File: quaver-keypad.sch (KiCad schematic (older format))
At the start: 14 parts

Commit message: MCU schematic fix
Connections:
- wire segments 51 -> 45
- no-connect marks 2 -> 0
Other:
- moved on the sheet: C?, R?, SW?, U?, Y?

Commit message: schematics finished
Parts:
- added D1, D2, D3, D4: D_Small, Diode_SMD:D_SOD-123, symbol Device:D_Small
- added F1: 500mA, Fuse:Fuse_1206_3216Metric, symbol Device:Polyfuse
- added MX1, MX2, MX3, MX4: MX-NoLED, MX_Alps_Hybrid:MX-1U, symbol MX_Alps_Hybrid:MX-NoLED
- added USB1: Molex-0548190589, random-keyboard-parts:Molex-0548190589, symbol random-keyboard-parts:Molex-0548190589
- C1, C2, C3, C4, C5, C6, C7: renamed from C?; footprint (none) -> Capacitor_SMD:C_0805_2012Metric
- R1, R2, R3, R4: renamed from R?; footprint (none) -> Resistor_SMD:R_0805_2012Metric
- SW1: renamed from SW?; footprint (none) -> random-keyboard-parts:SKQG-1155865
- Y1: renamed from Y?; footprint (none) -> Crystal:Crystal_SMD_3225-4Pin_3.2x2.5mm
- gave numbers to parts that had none: 1
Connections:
- net +5V: now also F1.1; no longer U1.24 (AVCC), U1.44 (AVCC)
- net D+: now also USB1.3 (D+)
- net D-: now also USB1.4 (D-)
- net GND: now also USB1.1 (GND); no longer U1.15 (GND), U1.23 (GND), U1.35 (GND), U1.43 (GND)
- net ROW0: now reaches U1.27 (PD7)
- net ROW0: now also D1.1 (K), D3.1 (K)
- net COL1: now reaches U1.28 (PB4)
- net COL1: now also MX3.1 (COL), MX4.1 (COL)
- net COL0: now reaches U1.29 (PB5)
- net COL0: now also MX1.1 (COL), MX2.1 (COL)
- net ROW1: now reaches U1.30 (PB6)
- net ROW1: now also D2.1 (K), D4.1 (K)
- new net: U1.15 (GND), U1.23 (GND), U1.35 (GND), U1.43 (GND)
- new net: U1.24 (AVCC), U1.44 (AVCC)
- new net: D1.2 (A), MX1.2 (ROW)
- new net: D3.2 (A), MX3.2 (ROW)
- new net: D2.2 (A), MX2.2 (ROW)
- new net: D4.2 (A), MX4.2 (ROW)
- new net VCC: F1.2, USB1.5 (VBUS)
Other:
- moved on the sheet: C1, C2, C3, C4, C5, C6, C7, R1, R2, R3, R4, SW1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

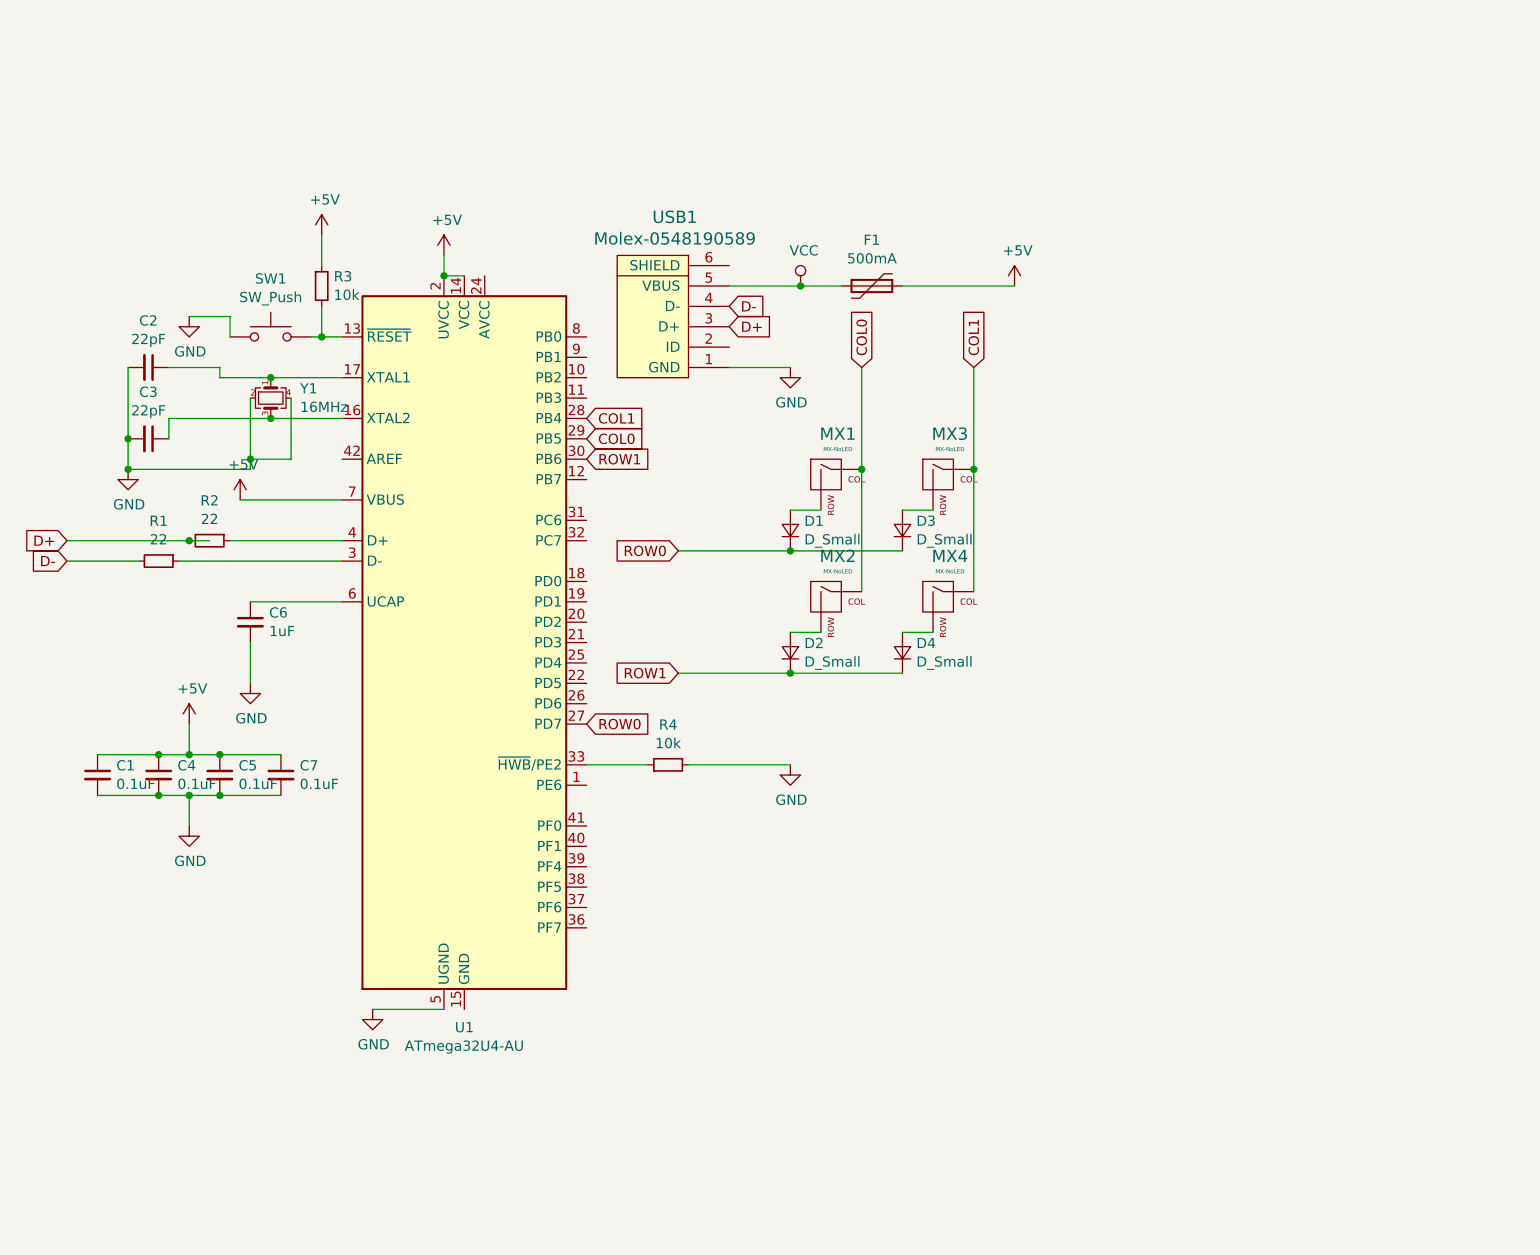
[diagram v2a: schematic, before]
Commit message: fixed mx keys
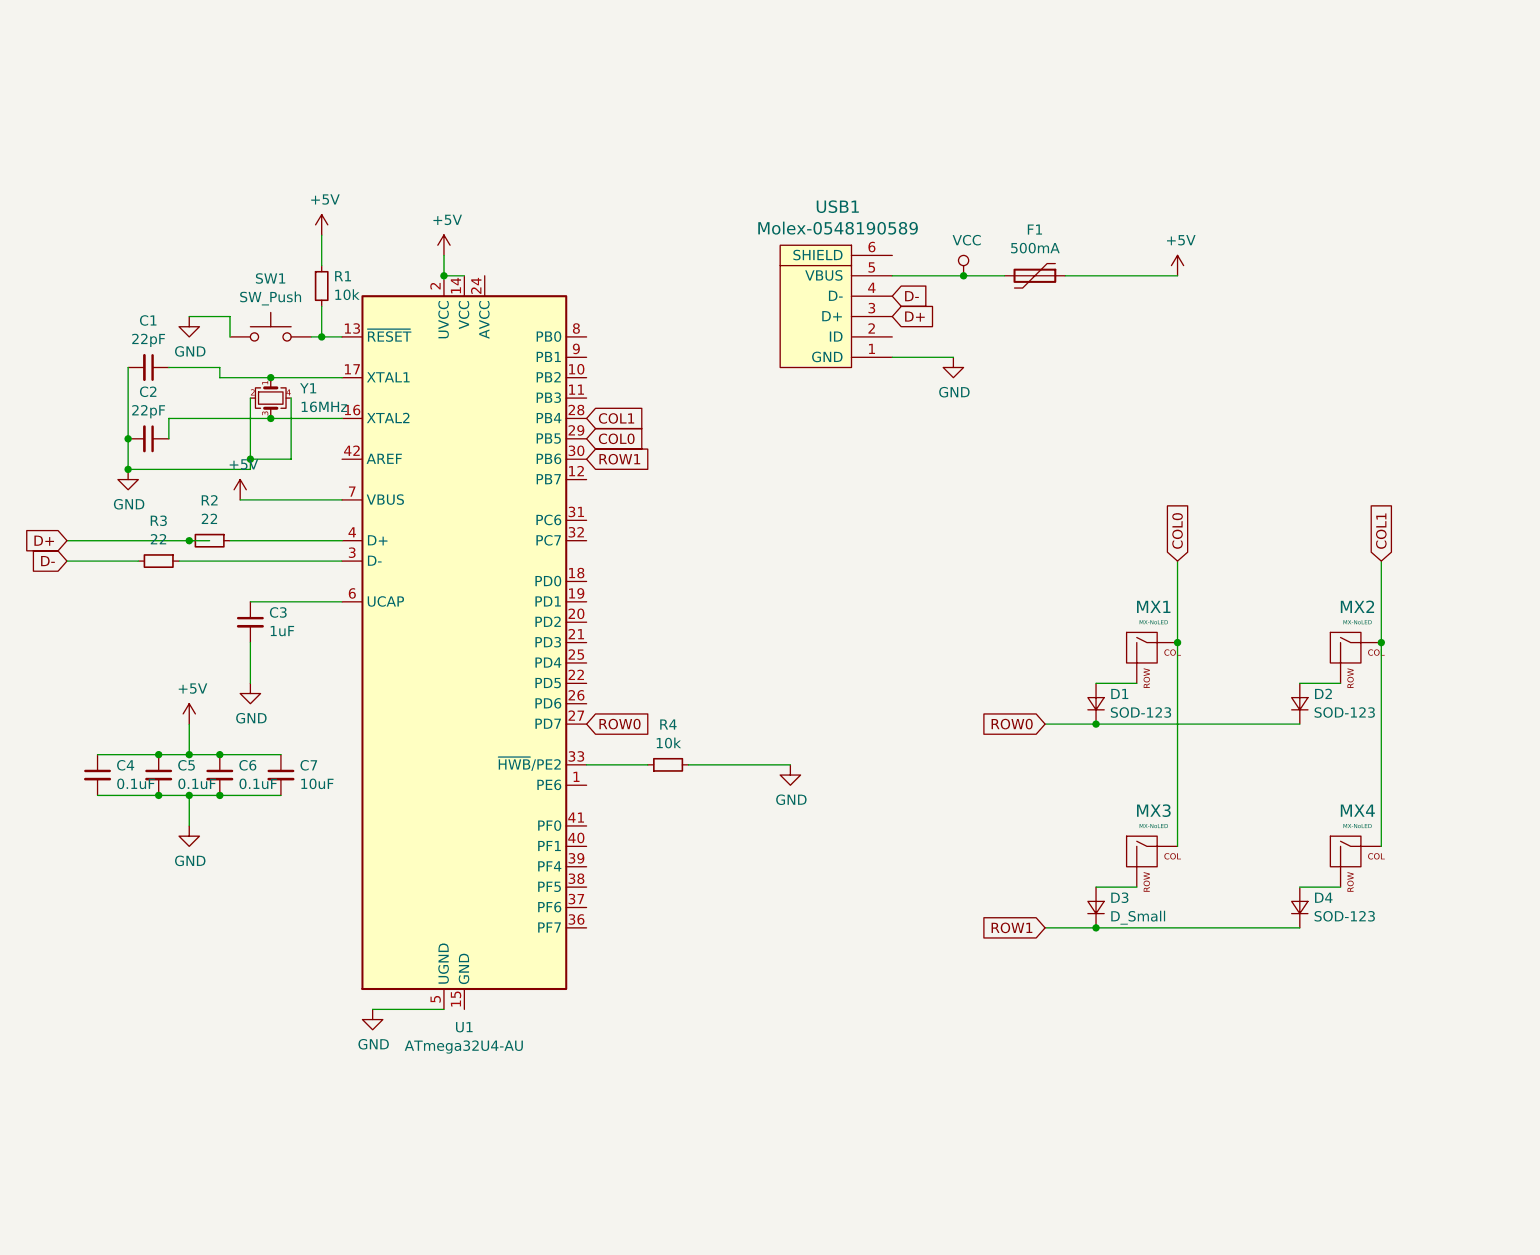
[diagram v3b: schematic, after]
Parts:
- C7: value 0.1uF -> 10uF
- D1, D2, D4: value D_Small -> SOD-123
- renumbered C2 to C1, C3 to C2, C6 to C3, C1 to C4, C4 to C5, C5 to C6, R3 to R1, R1 to R3
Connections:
- net COL0: now also MX3.1 (COL); no longer MX2.1 (COL)
- net COL1: now also MX2.1 (COL); no longer MX3.1 (COL)
- net ROW0: now also D2.1 (K); no longer D3.1 (K)
- net ROW1: now also D3.1 (K); no longer D2.1 (K)
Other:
- moved on the sheet: F1, USB1

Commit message: finished general pcb
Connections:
- net +5V: now also U1.24 (AVCC), U1.44 (AVCC)
- net GND: now also U1.15 (GND), U1.23 (GND), U1.35 (GND), U1.43 (GND)
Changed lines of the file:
@@
 Wire Wire Line
 	7900 3950 7900 4950
+Wire Wire Line
+	4400 5750 4300 5750
+Connection ~ 4300 5750
+Wire Wire Line
+	4500 2150 4400 2150
+Connection ~ 4400 2150
 $EndSCHEMATC
